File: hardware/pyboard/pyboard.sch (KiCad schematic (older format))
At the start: 2 parts

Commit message: Create schematic
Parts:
- added J?: Micro_SD_Card_Det, symbol Connector:Micro_SD_Card_Det
- added J?: USB_B_Micro, symbol Connector:USB_B_Micro
- added U?: MIC2005A-1YM5, symbol components:MIC2005A-1YM5
- added U?: MMA7660FC, symbol components:MMA7660FC
- added U?: MCP1703A-3302_SOT89, Package_TO_SOT_SMD:SOT-89-3, symbol Regulator_Linear:MCP1703A-3302_SOT89
- added Y?: Crystal_GND3_Small, symbol Device:Crystal_GND3_Small
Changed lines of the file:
@@
+	1    0    0    -1
+$EndComp
+$Comp
+L Connector:Micro_SD_Card_Det J?
+U 1 1 5D80F0E7
+P 9800 1600
+F 0 "J?" H 9750 2417 50  0000 C CNN
+F 1 "Micro_SD_Card_Det" H 9750 2326 50  0000 C CNN
+F 2 "" H 11850 2300 50  0001 C CNN
+F 3 "https://www.hirose.com/product/en/download_file/key_name/DM3/category/Catalog/doc_file_id/49662/?file_category_id=4&item_id=195&is_series=1" H 9800 1700 50  0001 C CNN
+	1    9800 1600
+	1    0    0    -1
+$EndComp
+$Comp
+L components:MIC2005A-1YM5 U?
+U 1 1 5D812FDB
+P 9650 4500
+F 0 "U?" H 9650 4867 50  0000 C CNN
+F 1 "MIC2005A-1YM5" H 9650 4776 50  0000 C CNN
+F 2 "" H 9650 4500 50  0001 C CNN
+F 3 "" H 9650 4500 50  0001 C CNN
+	1    9650 4500
+	1    0    0    -1
+$EndComp
+$Comp
+L components:MMA7660FC U?
+U 1 1 5D815AE2
+P 6000 5000
+F 0 "U?" H 6000 5465 50  0000 C CNN
+F 1 "MMA7660FC" H 6000 5374 50  0000 C CNN
+F 2 "" H 5700 5300 50  0001 C CNN
+F 3 "https://www.nxp.com/docs/en/data-sheet/MMA7660FC.pdf" H 5700 5300 50  0001 C CNN
+	1    6000 5000
+	1    0    0    -1
+$EndComp
+$Comp
+L Connector:USB_B_Micro J?
+U 1 1 5D8179A9
+P 10050 3450
+F 0 "J?" H 10107 3917 50  0000 C CNN
+F 1 "USB_B_Micro" H 10107 3826 50  0000 C CNN
+F 2 "" H 10200 3400 50  0001 C CNN
+F 3 "~" H 10200 3400 50  0001 C CNN
+	1    10050 3450
+	1    0    0    -1
+$EndComp
+$Comp
+L Regulator_Linear:MCP1703A-3302_SOT89 U?
+U 1 1 5D818CF7
+P 2150 6800
+F 0 "U?" H 2150 7042 50  0000 C CNN
+F 1 "MCP1703A-3302_SOT89" H 2150 6951 50  0000 C CNN
+F 2 "Package_TO_SOT_SMD:SOT-89-3" H 2150 7000 50  0001 C CNN
+F 3 "http://ww1.microchip.com/downloads/en/DeviceDoc/20005122B.pdf" H 2150 6750 50  0001 C CNN
+	1    2150 6800
+	1    0    0    -1
+$EndComp
+$Comp
+L Device:Crystal_GND3_Small Y?
+U 1 1 5D81BBD5
+P 3350 6250
+F 0 "Y?" H 3350 6475 50  0000 C CNN
+F 1 "Crystal_GND3_Small" H 3350 6384 50  0000 C CNN
+F 2 "" H 3350 6250 50  0001 C CNN
+F 3 "~" H 3350 6250 50  0001 C CNN
+	1    3350 6250
 	1    0    0    -1
 $EndComp

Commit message: Add microsd schematic
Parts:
- removed U? (x2): STM32F405RGT6, symbol components:STM32F405RGT6
- removed Y?: Crystal_GND3_Small, symbol Device:Crystal_GND3_Small
- added C? (x3): 2.2uF, symbol Device:C
- added C? (x4): 4.7uF, symbol Device:C
- added C? (x9): 100nF, symbol Device:C
- added C? (x2): 10pF, symbol Device:C
- added D?: MSE1PB-M3/89A, symbol Device:D
- added J?: Battery, symbol Connector_Generic:Conn_01x02
- added L?: 1uH, symbol Device:L
- added Q?: DMP2165UW, symbol components:DMP2165UW
- added R? (x2): 4k7, symbol Device:R
- added R? (x2): 100k, symbol Device:R
- added R? (x2): 22, symbol Device:R
- added R? (x2): 560, symbol Device:R
- added SW? (x2): SW_Push_Dual, symbol Switch:SW_Push_Dual
- added U? (x2): STM32F405RGT6, symbol components:STM32F405RGT6
- added U? (x2): STM32F405RGT6, symbol pyboard-rescue:STM32F405RGT6-components
- added Y?: 12MHz, symbol Device:Crystal_GND24
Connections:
- net labels added: +3.3V, +BATT, B, BOOT0, GND, PA10-ID, PA11-D-, PA12-D+, PA8-SDIO_SW, PA9-VBUS, PB2-BOOT1-INT, PB3-SW, PB5-MMA_AVDD, PB6-SCL, PB7-SDA, PC10-SDIO_D2, PC11-SDIO_D3, PC12-SIDO_CK, PC8-SDIO_D0, PC9-SDIO_D1, PD2-SDIO_CMD, USR-SW, VBUS, VCAP_1, VCAP_2, VCC, VDDA, VRTC, ~RST
- wire segments 0 -> 167
- no-connect marks 0 -> 5
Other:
- note added: "Calculate inductance value!!!\n"
- note added: "Which detection line should be used???\n"
- moved on the sheet: J?, U?

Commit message: Add ports
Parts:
- added C? (x2): 2.2pF, symbol Device:C
- added D?: LED_RED, symbol Device:LED_ALT
- added D?: LED_GREEN, symbol Device:LED_ALT
- added D?: LED_YELLOW, symbol Device:LED_ALT
- added D?: LED_BLUE, symbol Device:LED_ALT
- added J? (x6): Conn_01x08, symbol Connector_Generic:Conn_01x08
- added J?: Conn_02x04, symbol Connector_Generic:Conn_02x04_Counter_Clockwise
- added R? (x3): 560, symbol Device:R
- added R?: 220, symbol Device:R
- added R? (x5): 4k7, symbol Device:R
- added R? (x4): 100k, symbol Device:R
- added Y?: 32.768kHz, symbol Device:Crystal_Small
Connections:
- net labels added: BOOT0-P1, G, N1, N2, PA-12DP, PA0-X1, PA1-X2, PA11-DM, PA12-DP, PA13-RED-P5, PA14-GRN-P4, PA15-YEL-P3, PA2-X3, PA3-X4, PA4-X5, PA5-X6, PA6-X7, PA7-X8, PB0-Y11, PB1-Y12, PB10-Y9, PB11-Y10, PB12-Y5, PB13-Y6, PB14-Y7, PB15-Y8, PB2-BOOT1-MMA-INT, PB3-SW-X17, PB4-BLU-P2, PB6-SCL-X9, PB7-SDA-X10, PB8-Y3, PB9-Y4, PC0-X19, PC1-X20, PC12-SDIO_CK, PC13-X18, PC2-X21, PC3-X22, PC4-X11, PC5-X12, PC6-Y1, PC7-Y2, R, VRSTIN, Y
- net labels removed: PA11-D-, PA12-D+, PB2-BOOT1-INT, PB3-SW
- wire segments 167 -> 335
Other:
- note added: "I2C pullups\n"
- moved on the sheet: C?, D?, J?, L?, Q?, R?, SW?, U?, U?A, U?B, U?C, Y?

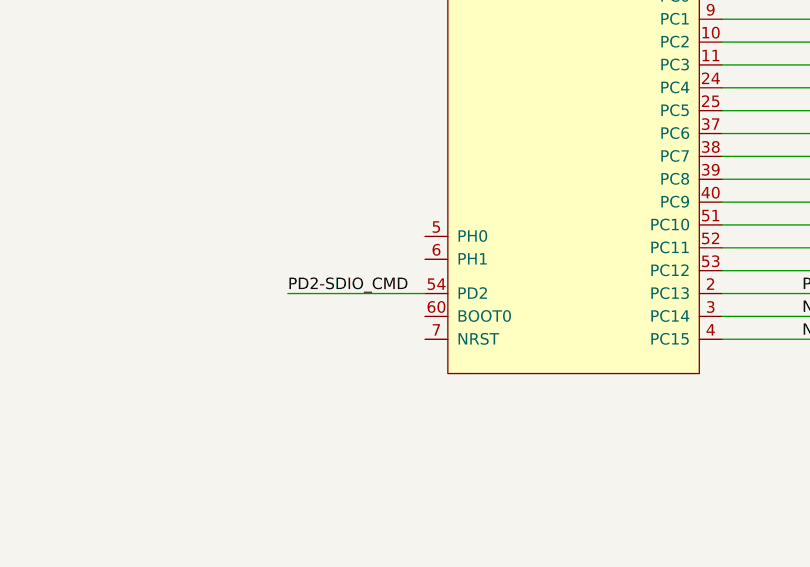
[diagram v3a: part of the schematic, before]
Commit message: Fix stm symbol
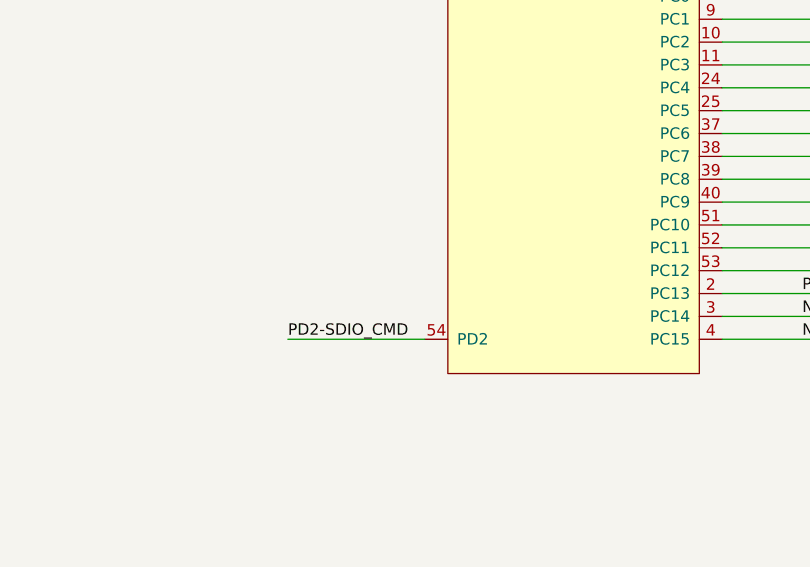
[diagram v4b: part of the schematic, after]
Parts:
- removed U?: STM32F405RGT6, symbol pyboard-rescue:STM32F405RGT6-components
- added U?: STM32F405RGT6, symbol components:STM32F405RGT6
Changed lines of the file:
@@
-$Comp
-L pyboard-rescue:STM32F405RGT6-components U?
-U 1 1 5D82FBBC
-P 4250 2800
-F 0 "U?" H 4250 4715 50  0000 C CNN
-F 1 "STM32F405RGT6" H 4250 4624 50  0000 C CNN
-F 2 "" H 4250 2650 50  0001 C CNN
-F 3 "https://www.st.com/resource/en/datasheet/dm00037051.pdf" H 4250 2650 50  0001 C CNN
-	1    4250 2800
-	1    0    0    -1
-$EndComp
 $Comp
 L pyboard-rescue:STM32F405RGT6-components U?
@@
 	4900 4150 5650 4150
 Wire Wire Line
-	3600 4150 3000 4150
-Text Label 3000 4150 0    50   ~ 0
+	3600 4350 3000 4350
+Text Label 3000 4350 0    50   ~ 0
 PD2-SDIO_CMD
 Text Label 5250 4150 0    50   ~ 0
@@
 Wire Wire Line
 	2350 2200 3600 2200
+$Comp
+L components:STM32F405RGT6 U?
+U 1 1 5D870B18
+P 4250 2800
+F 0 "U?" H 4250 4715 50  0000 C CNN
+F 1 "STM32F405RGT6" H 4250 4624 50  0000 C CNN
+F 2 "" H 4250 2650 50  0001 C CNN
+F 3 "https://www.st.com/resource/en/datasheet/dm00037051.pdf" H 4250 2650 50  0001 C CNN
+	1    4250 2800
+	1    0    0    -1
+$EndComp
 $EndSCHEMATC

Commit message: Fix ferrite bead symbol
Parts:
- removed L?: 1uH, symbol Device:L
- removed R? (x2): 100k, symbol Device:R
- added FB?: 1k, symbol Device:Ferrite_Bead
- added R? (x2): 100k, symbol Device:R
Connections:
- wire segments 335 -> 333
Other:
- moved on the sheet: R?
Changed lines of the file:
@@
 Wire Wire Line
 	4900 10400 4900 10450
-$Comp
-L Device:L L?
-U 1 1 5D840409
-P 3950 10050
-F 0 "L?" V 4140 10050 50  0000 C CNN
-F 1 "1uH " V 4049 10050 50  0000 C CNN
-F 2 "" H 3950 10050 50  0001 C CNN
-F 3 "~" H 3950 10050 50  0001 C CNN
-	1    3950 10050
-	0    -1   -1   0
-$EndComp
 Wire Wire Line
 	4450 10050 4100 10050
@@
 Wire Wire Line
 	5950 2600 4900 2600
-$Comp
-L Device:R R?
-U 1 1 5DE16C77
-P 6150 2500
-F 0 "R?" H 6220 2546 50  0000 L CNN
-F 1 "100k" H 6220 2455 50  0000 L CNN
-F 2 "" V 6080 2500 50  0001 C CNN
-F 3 "~" H 6150 2500 50  0001 C CNN
-	1    6150 2500
-	1    0    0    -1
-$EndComp
-$Comp
-L Device:R R?
-U 1 1 5DE16FB8
-P 6500 2500
-F 0 "R?" H 6570 2546 50  0000 L CNN
-F 1 "100k" H 6570 2455 50  0000 L CNN
-F 2 "" V 6430 2500 50  0001 C CNN
-F 3 "~" H 6500 2500 50  0001 C CNN
-	1    6500 2500
-	1    0    0    -1
-$EndComp
-$Comp
-L power:GND #PWR?
-U 1 1 5DE31D90
-P 6150 2800
-F 0 "#PWR?" H 6150 2550 50  0001 C CNN
-F 1 "GND" H 6155 2627 50  0000 C CNN
-F 2 "" H 6150 2800 50  0001 C CNN
-F 3 "" H 6150 2800 50  0001 C CNN
-	1    6150 2800
-	1    0    0    -1
-$EndComp
-Wire Wire Line
-	6150 2800 6150 2700
-Wire Wire Line
-	6150 2700 6500 2700
-Wire Wire Line
-	6500 2700 6500 2650
-Connection ~ 6150 2700
-Wire Wire Line
-	6150 2700 6150 2650
-Wire Wire Line
-	6150 1700 6150 2350
-Wire Wire Line
-	4900 1700 6150 1700
-Wire Wire Line
-	6500 1400 6500 2350
 Wire Wire Line
 	4900 1400 6500 1400
@@
 L Device:R R?
 U 1 1 5DE9D5AC
-P 7000 1400
-F 0 "R?" H 7070 1446 50  0000 L CNN
-F 1 "4k7" H 7070 1355 50  0000 L CNN
-F 2 "" V 6930 1400 50  0001 C CNN
-F 3 "~" H 7000 1400 50  0001 C CNN
-	1    7000 1400
+P 7690 1400
+F 0 "R?" H 7760 1446 50  0000 L CNN
+F 1 "4k7" H 7760 1355 50  0000 L CNN
+F 2 "" V 7620 1400 50  0001 C CNN
+F 3 "~" H 7690 1400 50  0001 C CNN
+	1    7690 1400
 	1    0    0    -1
 $EndComp
@@
 L Device:R R?
 U 1 1 5DE9F317
-P 7300 1400
-F 0 "R?" H 7370 1446 50  0000 L CNN
-F 1 "4k7" H 7370 1355 50  0000 L CNN
-F 2 "" V 7230 1400 50  0001 C CNN
-F 3 "~" H 7300 1400 50  0001 C CNN
-	1    7300 1400
+P 7990 1400
+F 0 "R?" H 8060 1446 50  0000 L CNN
+F 1 "4k7" H 8060 1355 50  0000 L CNN
+F 2 "" V 7920 1400 50  0001 C CNN
+F 3 "~" H 7990 1400 50  0001 C CNN
+	1    7990 1400
 	1    0    0    -1
 $EndComp
@@
 L Device:R R?
 U 1 1 5DE9F562
-P 7600 1400
-F 0 "R?" H 7670 1446 50  0000 L CNN
-F 1 "4k7" H 7670 1355 50  0000 L CNN
-F 2 "" V 7530 1400 50  0001 C CNN
-F 3 "~" H 7600 1400 50  0001 C CNN
-	1    7600 1400
+P 8290 1400
+F 0 "R?" H 8360 1446 50  0000 L CNN
+F 1 "4k7" H 8360 1355 50  0000 L CNN
+F 2 "" V 8220 1400 50  0001 C CNN
+F 3 "~" H 8290 1400 50  0001 C CNN
+	1    8290 1400
 	1    0    0    -1
 $EndComp
@@
 L Device:R R?
 U 1 1 5DE9F750
-P 7900 1400
-F 0 "R?" H 7970 1446 50  0000 L CNN
-F 1 "4k7" H 7970 1355 50  0000 L CNN
-F 2 "" V 7830 1400 50  0001 C CNN
-F 3 "~" H 7900 1400 50  0001 C CNN
-	1    7900 1400
-	1    0    0    -1
-$EndComp
-Wire Wire Line
-	7000 1550 7000 1800
-Wire Wire Line
-	4900 1800 7000 1800
-Wire Wire Line
-	7300 1550 7300 1900
-Wire Wire Line
-	4900 1900 7300 1900
-Wire Wire Line
-	7600 1550 7600 2200
-Wire Wire Line
-	4900 2200 7600 2200
-Wire Wire Line
-	7900 1550 7900 2300
-Wire Wire Line
-	4900 2300 7900 2300
+P 8590 1400
+F 0 "R?" H 8660 1446 50  0000 L CNN
+F 1 "4k7" H 8660 1355 50  0000 L CNN
+F 2 "" V 8520 1400 50  0001 C CNN
+F 3 "~" H 8590 1400 50  0001 C CNN
+	1    8590 1400
+	1    0    0    -1
+$EndComp
+Wire Wire Line
+	7690 1550 7690 1800
+Wire Wire Line
+	7990 1550 7990 1900
+Wire Wire Line
+	8290 1550 8290 2200
+Wire Wire Line
+	8590 1550 8590 2300
 $Comp
 L power:+3.3V #PWR?
 U 1 1 5DF0D113
-P 6700 1100
-F 0 "#PWR?" H 6700 950 50  0001 C CNN
-F 1 "+3.3V" H 6715 1273 50  0000 C CNN
-F 2 "" H 6700 1100 50  0001 C CNN
-F 3 "" H 6700 1100 50  0001 C CNN
-	1    6700 1100
-	1    0    0    -1
-$EndComp
-Wire Wire Line
-	7900 1250 7600 1250
-Wire Wire Line
-	6700 1250 6700 1100
-Connection ~ 7000 1250
-Wire Wire Line
-	7000 1250 6700 1250
-Connection ~ 7300 1250
-Wire Wire Line
-	7300 1250 7000 1250
-Connection ~ 7600 1250
-Wire Wire Line
-	7600 1250 7300 1250
-Text Notes 7200 1150 0    50   ~ 0
+P 7390 1100
+F 0 "#PWR?" H 7390 950 50  0001 C CNN
+F 1 "+3.3V" H 7405 1273 50  0000 C CNN
+F 2 "" H 7390 1100 50  0001 C CNN
+F 3 "" H 7390 1100 50  0001 C CNN
+	1    7390 1100
+	1    0    0    -1
+$EndComp
+Wire Wire Line
+	8590 1250 8290 1250
+Wire Wire Line
+	7390 1250 7390 1100
+Connection ~ 7690 1250
+Wire Wire Line
+	7690 1250 7390 1250
+Connection ~ 7990 1250
+Wire Wire Line
+	7990 1250 7690 1250
+Connection ~ 8290 1250
+Wire Wire Line
+	8290 1250 7990 1250
+Text Notes 7890 1150 0    50   ~ 0
 I2C pullups\n
 Text Label 2900 1200 0    50   ~ 0
@@
 	2350 2200 3600 2200
 $Comp
+L Device:Ferrite_Bead FB?
+U 1 1 5D8BB4E5
+P 3950 10050
+F 0 "FB?" V 4224 10050 50  0000 C CNN
+F 1 "1k" V 4133 10050 50  0000 C CNN
+F 2 "" V 3880 10050 50  0001 C CNN
+F 3 "~" H 3950 10050 50  0001 C CNN
+	1    3950 10050
+	0    -1   -1   0
+$EndComp
+$Comp
+L Device:R R?
+U 1 1 5D90C247
+P 6650 1400
+F 0 "R?" V 6443 1400 50  0000 C CNN
+F 1 "100k" V 6534 1400 50  0000 C CNN
+F 2 "" V 6580 1400 50  0001 C CNN
+F 3 "~" H 6650 1400 50  0001 C CNN
+	1    6650 1400
+	0    1    1    0
+$EndComp
+$Comp
+L Device:R R?
+U 1 1 5D90DB32
+P 6650 1700
+F 0 "R?" V 6443 1700 50  0000 C CNN
+F 1 "100k" V 6534 1700 50  0000 C CNN
+F 2 "" V 6580 1700 50  0001 C CNN
+F 3 "~" H 6650 1700 50  0001 C CNN
+	1    6650 1700
+	0    1    1    0
+$EndComp
+Wire Wire Line
+	4900 1700 6500 1700
+Wire Wire Line
+	7100 1700 7100 1400
+Wire Wire Line
+	7100 1400 6800 1400
+Wire Wire Line
+	6800 1700 7100 1700
+$Comp
+L power:GND #PWR?
+U 1 1 5D977795
+P 7300 1400
+F 0 "#PWR?" H 7300 1150 50  0001 C CNN
+F 1 "GND" H 7305 1227 50  0000 C CNN
+F 2 "" H 7300 1400 50  0001 C CNN
+F 3 "" H 7300 1400 50  0001 C CNN
+	1    7300 1400
+	1    0    0    -1
+$EndComp
+Wire Wire Line
+	7100 1400 7300 1400
+Connection ~ 7100 1400
+Wire Wire Line
+	4900 1800 7690 1800
+Wire Wire Line
+	4900 1900 7990 1900
+Wire Wire Line
+	4900 2200 8290 2200
+Wire Wire Line
+	4900 2300 8590 2300
+$Comp
 L components:STM32F405RGT6 U?

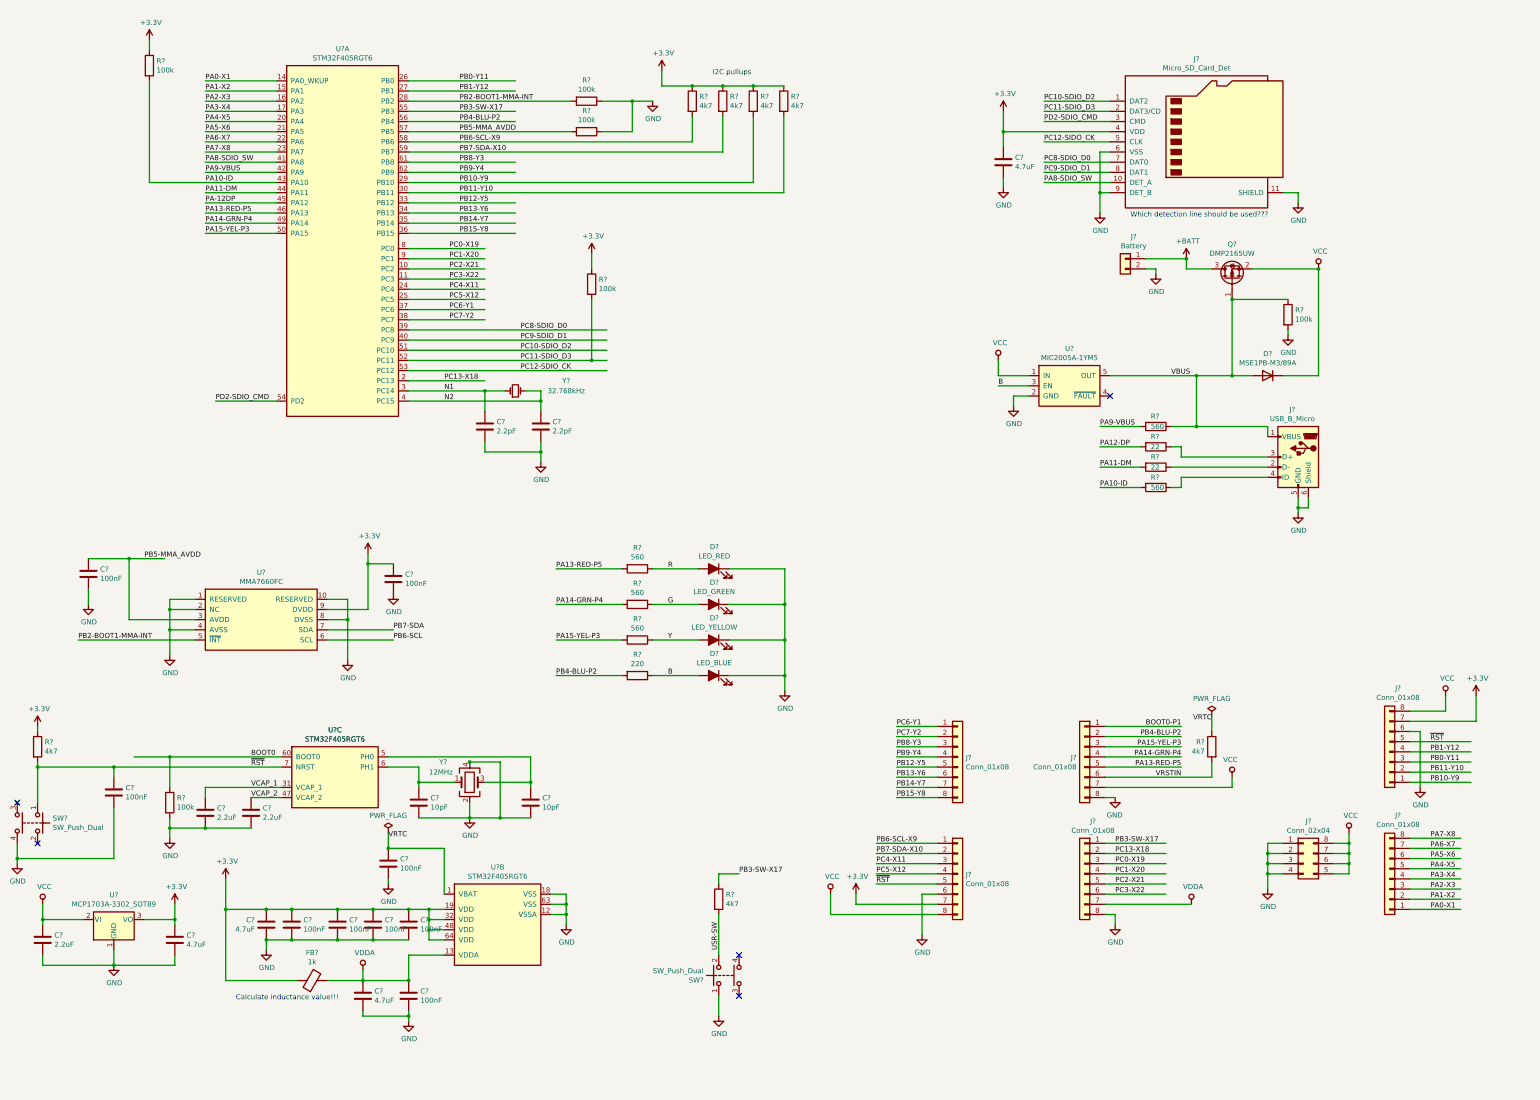
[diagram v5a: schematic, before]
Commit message: Group symbols by blocks
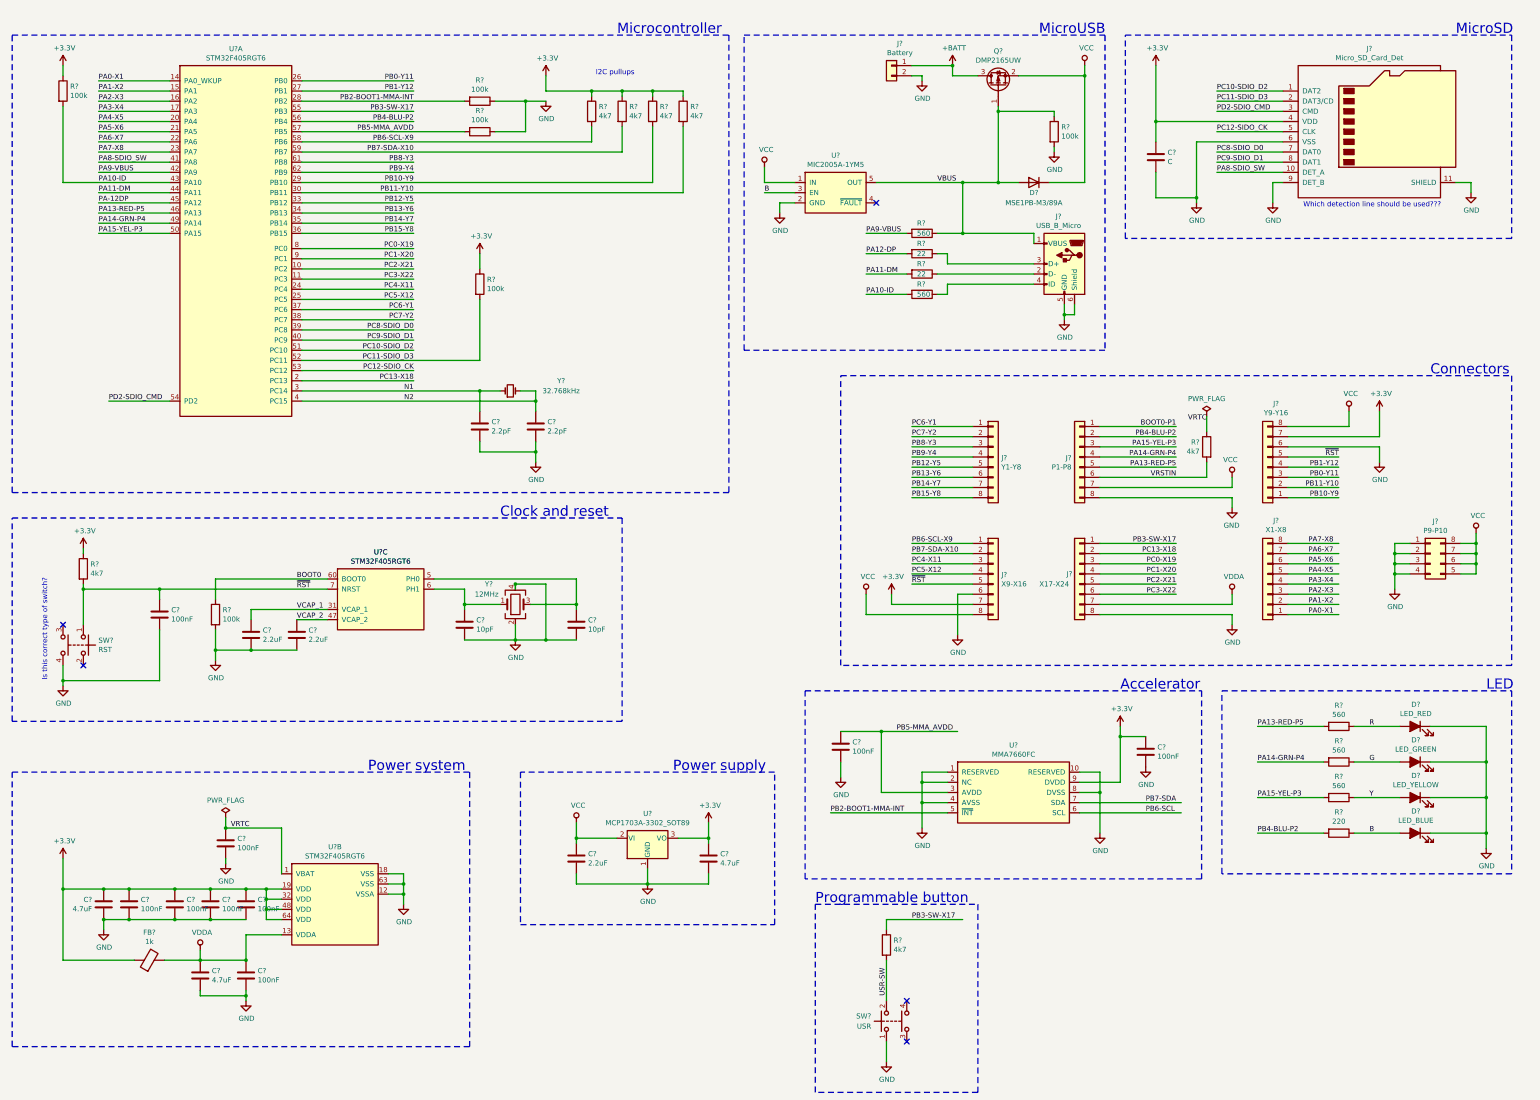
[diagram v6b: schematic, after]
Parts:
- removed C?: 4.7uF, symbol Device:C
- removed R? (x4): 4k7, symbol Device:R
- added C?: C, symbol Device:C
- added R? (x4): 4k7, symbol Device:R
- J?: value Conn_01x08 -> Y1-Y8
- J?: value Conn_01x08 -> X9-X16
- J?: value Conn_01x08 -> P1-P8
- J?: value Conn_01x08 -> X17-X24
- J?: value Conn_02x04 -> P9-P10
- J?: value Conn_01x08 -> Y9-Y16
- J?: value Conn_01x08 -> X1-X8
- SW?: value SW_Push_Dual -> RST
- SW?: value SW_Push_Dual -> USR
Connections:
- wire segments 333 -> 342
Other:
- note added: "Accelerator\n"
- note added: "Clock and reset\n"
- note added: "Connectors"
- note added: "Is this correct type of switch?\n"
- note added: "LED"
- note added: "MicroSD"
- note added: "MicroUSB"
- note added: "Microcontroller"
- note added: "Power supply"
- note added: "Power system"
- note added: "Programmable button"
- note removed: "Calculate inductance value!!!\n"
- moved on the sheet: C?, D?, FB?, J?, Q?, R?, SW?, U?, U?A, U?B, U?C, Y?
